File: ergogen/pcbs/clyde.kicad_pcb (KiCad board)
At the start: 2 copper layers, 111.4 x 85.7 mm, 24 parts

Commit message: prototypes ordered
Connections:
- TRRS1 pad 4: GP12 -> GP16
- U0 pad 10: matrix_middle_home -> matrix_inner_home
- U0 pad 11: matrix_middle_bottom -> matrix_inner_bottom
- U0 pad 12: matrix_index_top -> matrix_ring_bottom
- U0 pad 14: matrix_index_home -> matrix_ring_home
- U0 pad 15: matrix_index_bottom -> matrix_ring_top
- U0 pad 16: GP12 -> matrix_middle_top
- U0 pad 17: matrix_inner_bottom -> matrix_middle_home
- U0 pad 19: matrix_inner_home -> matrix_middle_bottom
- U0 pad 20: matrix_inner_top -> GP15
- U0 pad 21: thumbfan_far_home -> GP16
- U0 pad 22: thumbfan_home_home -> thumbfan_far_home
- U0 pad 24: thumbfan_near_home -> thumbfan_home_home
- U0 pad 25: GP19 -> thumbfan_near_home
- U0 pad 5: matrix_ring_bottom -> matrix_index_bottom
- U0 pad 6: matrix_ring_home -> matrix_index_home
- U0 pad 7: matrix_ring_top -> matrix_index_top
- U0 pad 9: matrix_middle_top -> matrix_inner_top
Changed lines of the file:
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@@
 (net 18 "thumbfan_home_home")
 (net 19 "thumbfan_far_home")
-(net 20 "GP12")
-(net 21 "GP19")
+(net 20 "GP15")
+(net 21 "GP16")
 (net 22 "GP20")
 (net 23 "GP21")
@@
 (add_net "thumbfan_home_home")
 (add_net "thumbfan_far_home")
-(add_net "GP12")
-(add_net "GP19")
+(add_net "GP15")
+(add_net "GP16")
 (add_net "GP20")
 (add_net "GP21")
@@
     (pad "3" thru_hole rect (at 8.82 -19.05) (size 1.84 1.7) (drill oval 1.16 1.02) (layers *.Cu *.Mask) (net 2 "GND"))
     (pad "4" thru_hole oval (at 8.82 -16.51) (size 1.84 1.7) (drill oval 1.16 1.02) (layers *.Cu *.Mask) (net 1 "matrix_pinky_bottom"))
-    (pad "5" thru_hole oval (at 8.82 -13.97) (size 1.84 1.7) (drill oval 1.16 1.02) (layers *.Cu *.Mask) (net 5 "matrix_ring_bottom"))
-    (pad "6" thru_hole oval (at 8.82 -11.43) (size 1.84 1.7) (drill oval 1.16 1.02) (layers *.Cu *.Mask) (net 6 "matrix_ring_home"))
-    (pad "7" thru_hole oval (at 8.82 -8.89) (size 1.84 1.7) (drill oval 1.16 1.02) (layers *.Cu *.Mask) (net 7 "matrix_ring_top"))
+    (pad "5" thru_hole oval (at 8.82 -13.97) (size 1.84 1.7) (drill oval 1.16 1.02) (layers *.Cu *.Mask) (net 11 "matrix_index_bottom"))
+    (pad "6" thru_hole oval (at 8.82 -11.43) (size 1.84 1.7) (drill oval 1.16 1.02) (layers *.Cu *.Mask) (net 12 "matrix_index_home"))
+    (pad "7" thru_hole oval (at 8.82 -8.89) (size 1.84 1.7) (drill oval 1.16 1.02) (layers *.Cu *.Mask) (net 13 "matrix_index_top"))
     (pad "8" thru_hole rect (at 8.82 -6.35) (size 1.84 1.7) (drill oval 1.16 1.02) (layers *.Cu *.Mask) (net 2 "GND"))
-    (pad "9" thru_hole oval (at 8.82 -3.81) (size 1.84 1.7) (drill oval 1.16 1.02) (layers *.Cu *.Mask) (net 10 "matrix_middle_top"))
-    (pad "10" thru_hole oval (at 8.82 -1.27) (size 1.84 1.7) (drill oval 1.16 1.02) (layers *.Cu *.Mask) (net 9 "matrix_middle_home"))
-    (pad "11" thru_hole oval (at 8.82 1.27) (size 1.84 1.7) (drill oval 1.16 1.02) (layers *.Cu *.Mask) (net 8 "matrix_middle_bottom"))
-    (pad "12" thru_hole oval (at 8.82 3.81) (size 1.84 1.7) (drill oval 1.16 1.02) (layers *.Cu *.Mask) (net 13 "matrix_index_top"))
+    (pad "9" thru_hole oval (at 8.82 -3.81) (size 1.84 1.7) (drill oval 1.16 1.02) (layers *.Cu *.Mask) (net 16 "matrix_inner_top"))
+    (pad "10" thru_hole oval (at 8.82 -1.27) (size 1.84 1.7) (drill oval 1.16 1.02) (layers *.Cu *.Mask) (net 15 "matrix_inner_home"))
+    (pad "11" thru_hole oval (at 8.82 1.27) (size 1.84 1.7) (drill oval 1.16 1.02) (layers *.Cu *.Mask) (net 14 "matrix_inner_bottom"))
+    (pad "12" thru_hole oval (at 8.82 3.81) (size 1.84 1.7) (drill oval 1.16 1.02) (layers *.Cu *.Mask) (net 5 "matrix_ring_bottom"))
     (pad "13" thru_hole rect (at 8.82 6.35) (size 1.84 1.7) (drill oval 1.16 1.02) (layers *.Cu *.Mask) (net 2 "GND"))
-    (pad "14" thru_hole oval (at 8.82 8.89) (size 1.84 1.7) (drill oval 1.16 1.02) (layers *.Cu *.Mask) (net 12 "matrix_index_home"))
-    (pad "15" thru_hole oval (at 8.82 11.43) (size 1.84 1.7) (drill oval 1.16 1.02) (layers *.Cu *.Mask) (net 11 "matrix_index_bottom"))
-    (pad "16" thru_hole oval (at 8.82 13.97) (size 1.84 1.7) (drill oval 1.16 1.02) (layers *.Cu *.Mask) (net 20 "GP12"))
-    (pad "17" thru_hole oval (at 8.82 16.51) (size 1.84 1.7) (drill oval 1.16 1.02) (layers *.Cu *.Mask) (net 14 "matrix_inner_bottom"))
+    (pad "14" thru_hole oval (at 8.82 8.89) (size 1.84 1.7) (drill oval 1.16 1.02) (layers *.Cu *.Mask) (net 6 "matrix_ring_home"))
+    (pad "15" thru_hole oval (at 8.82 11.43) (size 1.84 1.7) (drill oval 1.16 1.02) (layers *.Cu *.Mask) (net 7 "matrix_ring_top"))
+    (pad "16" thru_hole oval (at 8.82 13.97) (size 1.84 1.7) (drill oval 1.16 1.02) (layers *.Cu *.Mask) (net 10 "matrix_middle_top"))
+    (pad "17" thru_hole oval (at 8.82 16.51) (size 1.84 1.7) (drill oval 1.16 1.02) (layers *.Cu *.Mask) (net 9 "matrix_middle_home"))
     (pad "18" thru_hole rect (at 8.82 19.05) (size 1.84 1.7) (drill oval 1.16 1.02) (layers *.Cu *.Mask) (net 2 "GND"))
-    (pad "19" thru_hole oval (at 8.82 21.59) (size 1.84 1.7) (drill oval 1.16 1.02) (layers *.Cu *.Mask) (net 15 "matrix_inner_home"))
-    (pad "20" thru_hole oval (at 8.82 24.13) (size 1.84 1.7) (drill oval 1.16 1.02) (layers *.Cu *.Mask) (net 16 "matrix_inner_top"))
-    (pad "21" thru_hole oval (at -8.82 24.13) (size 1.84 1.7) (drill oval 1.16 1.02) (layers *.Cu *.Mask) (net 19 "thumbfan_far_home"))
-    (pad "22" thru_hole oval (at -8.82 21.59) (size 1.84 1.7) (drill oval 1.16 1.02) (layers *.Cu *.Mask) (net 18 "thumbfan_home_home"))
+    (pad "19" thru_hole oval (at 8.82 21.59) (size 1.84 1.7) (drill oval 1.16 1.02) (layers *.Cu *.Mask) (net 8 "matrix_middle_bottom"))
+    (pad "20" thru_hole oval (at 8.82 24.13) (size 1.84 1.7) (drill oval 1.16 1.02) (layers *.Cu *.Mask) (net 20 "GP15"))
+    (pad "21" thru_hole oval (at -8.82 24.13) (size 1.84 1.7) (drill oval 1.16 1.02) (layers *.Cu *.Mask) (net 21 "GP16"))
+    (pad "22" thru_hole oval (at -8.82 21.59) (size 1.84 1.7) (drill oval 1.16 1.02) (layers *.Cu *.Mask) (net 19 "thumbfan_far_home"))
     (pad "23" thru_hole rect (at -8.82 19.05) (size 1.84 1.7) (drill oval 1.16 1.02) (layers *.Cu *.Mask) (net 2 "GND"))
-    (pad "24" thru_hole oval (at -8.82 16.51) (size 1.84 1.7) (drill oval 1.16 1.02) (layers *.Cu *.Mask) (net 17 "thumbfan_near_home"))
-    (pad "25" thru_hole oval (at -8.82 13.97) (size 1.84 1.7) (drill oval 1.16 1.02) (layers *.Cu *.Mask) (net 21 "GP19"))
+    (pad "24" thru_hole oval (at -8.82 16.51) (size 1.84 1.7) (drill oval 1.16 1.02) (layers *.Cu *.Mask) (net 18 "thumbfan_home_home"))
+    (pad "25" thru_hole oval (at -8.82 13.97) (size 1.84 1.7) (drill oval 1.16 1.02) (layers *.Cu *.Mask) (net 17 "thumbfan_near_home"))
     (pad "26" thru_hole oval (at -8.82 11.43) (size 1.84 1.7) (drill oval 1.16 1.02) (layers *.Cu *.Mask) (net 22 "GP20"))
     (pad "27" thru_hole oval (at -8.82 8.89) (size 1.84 1.7) (drill oval 1.16 1.02) (layers *.Cu *.Mask) (net 23 "GP21"))
@@
         (pad 2 thru_hole oval (at -4.6 10.2 0) (size 1.6 2.2) (drill oval 0.9 1.5) (layers *.Cu *.Mask) (net 2 "GND"))
         (pad 3 thru_hole oval (at -4.6 6.2 0) (size 1.6 2.2) (drill oval 0.9 1.5) (layers *.Cu *.Mask) (net 32 "VSYS"))
-        (pad 4 thru_hole oval (at -4.6 3.2 0) (size 1.6 2.2) (drill oval 0.9 1.5) (layers *.Cu *.Mask) (net 20 "GP12"))
+        (pad 4 thru_hole oval (at -4.6 3.2 0) (size 1.6 2.2) (drill oval 0.9 1.5) (layers *.Cu *.Mask) (net 21 "GP16"))
         (pad 1 thru_hole oval (at -4.6 11.3 0) (size 1.6 2.2) (drill oval 0.9 1.5) (layers *.Cu *.Mask) (net 2 "GND"))
         (pad 2 thru_hole oval (at 0 10.2 0) (size 1.6 2.2) (drill oval 0.9 1.5) (layers *.Cu *.Mask) (net 2 "GND"))
         (pad 3 thru_hole oval (at 0 6.2 0) (size 1.6 2.2) (drill oval 0.9 1.5) (layers *.Cu *.Mask) (net 32 "VSYS"))
-        (pad 4 thru_hole oval (at 0 3.2 0) (size 1.6 2.2) (drill oval 0.9 1.5) (layers *.Cu *.Mask) (net 20 "GP12"))
+        (pad 4 thru_hole oval (at 0 3.2 0) (size 1.6 2.2) (drill oval 0.9 1.5) (layers *.Cu *.Mask) (net 21 "GP16"))
       )
             (gr_text "JLCJLCJLCJLC" (at 190.5 123.825 0) (layer F.SilkS)

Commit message: layout like split weteor/Kong; outline tweaks
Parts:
- moved S16 4.76 mm to (209.6, 175.3)
- moved S17 4.76 mm to (228.6, 175.3)
- moved _4 4.76 mm to (238.1, 165.7)
- moved S18 4.39 mm to (247.7, 177.6)
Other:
- board size 111.4 x 85.7 mm -> 114.3 x 82.4 mm
- board text added: "clyde v0.0.2"
- board text removed: "clyde v0.0.1"
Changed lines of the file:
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@@
           )
       (module MX (layer F.Cu)
-      (at 206.69250000000002 179.07 0)
+      (at 209.55 175.26 0)
       (fp_text reference "S16" (at 0 0) (layer F.SilkS) hide (effects (font (size 1.27 1.27) (thickness 0.15))))
       (fp_text value "" (at 0 0) (layer F.SilkS) hide (effects (font (size 1.27 1.27) (thickness 0.15))))
@@
           )
       (module MX (layer F.Cu)
-      (at 225.74250000000004 179.07 0)
+      (at 228.60000000000002 175.26 0)
       (fp_text reference "S17" (at 0 0) (layer F.SilkS) hide (effects (font (size 1.27 1.27) (thickness 0.15))))
       (fp_text value "" (at 0 0) (layer F.SilkS) hide (effects (font (size 1.27 1.27) (thickness 0.15))))
@@
           )
       (module MX (layer F.Cu)
-      (at 244.79250000000002 180.975 0)
+      (at 247.65 177.64124999999999 0)
       (fp_text reference "S18" (at 0 0) (layer F.SilkS) hide (effects (font (size 1.27 1.27) (thickness 0.15))))
       (fp_text value "" (at 0 0) (layer F.SilkS) hide (effects (font (size 1.27 1.27) (thickness 0.15))))
@@
                 (effects (font (size 1 1) (thickness 0.15)) )
             )
-            (gr_text "clyde v0.0.1" (at 190.5 142.875 0) (layer F.SilkS)
+            (gr_text "clyde v0.0.2" (at 190.5 142.875 0) (layer F.SilkS)
                 (effects (font (size 1 1) (thickness 0.15)) )
             )
     (module "MountingHole_2.2mm_M2_Pad_Via" (version 20210722) (generator pcbnew) (layer "F.Cu")
-      (at 235.26750000000004 169.545 0)
+      (at 238.12500000000003 165.73499999999999 0)
       (fp_text reference "_4" (at 0 -3.2) (layer "F.SilkS") hide
         (effects (font (size 1 1) (thickness 0.15)))
@@
       (pad "1" thru_hole circle locked (at 0 -1.65) (size 0.7 0.7) (drill 0.4) (layers *.Cu *.Mask))
     )
-            (gr_line (start 142.875 182.88815625463917) (end 142.875 107.77499999999999) (angle 90) (layer Edge.Cuts) (width 0.15))
-(gr_line (start 145.875 104.77499999999999) (end 244.94297008970588 104.77499999999999) (angle 90) (layer Edge.Cuts) (width 0.15))
-(gr_line (start 247.92719999989208 107.46779999895125) (end 254.30172991018622 169.3918048418086) (angle 90) (layer Edge.Cuts) (width 0.15))
-(gr_line (start 254.31750000000002 169.699004842857) (end 254.31750000000002 187.5) (angle 90) (layer Edge.Cuts) (width 0.15))
-(gr_line (start 251.31750000000002 190.5) (end 235.34476865999997 190.5) (angle 90) (layer Edge.Cuts) (width 0.15))
-(gr_line (start 235.19033465459398 190.49602240487596) (end 145.720565994594 185.8841786595152) (angle 90) (layer Edge.Cuts) (width 0.15))
-(gr_arc (start 145.875 107.77499999999999) (end 145.875 104.77499999999999) (angle -90) (layer Edge.Cuts) (width 0.15))
-(gr_arc (start 244.94297008970588 107.77499999999999) (end 247.92719998970588 107.4678) (angle -84.1226099916367) (layer Edge.Cuts) (width 0.15))
-(gr_arc (start 251.31750000000002 169.699004842857) (end 254.31750000000002 169.699004842857) (angle -5.877390008356565) (layer Edge.Cuts) (width 0.15))
-(gr_arc (start 251.31750000000002 187.5) (end 251.31750000000002 190.5) (angle -90) (layer Edge.Cuts) (width 0.15))
-(gr_arc (start 235.34476865999997 187.5) (end 235.19033465999996 190.4960224) (angle -2.9507764544792394) (layer Edge.Cuts) (width 0.15))
-(gr_arc (start 145.875 182.88815625463917) (end 142.875 182.88815625463917) (angle -87.04922354552087) (layer Edge.Cuts) (width 0.15))
+            (gr_line (start 142.875 185.16625) (end 142.875 106.77499999999999) (angle 90) (layer Edge.Cuts) (width 0.15))
+(gr_line (start 144.875 104.77499999999999) (end 245.65000000000003 104.77499999999999) (angle 90) (layer Edge.Cuts) (width 0.15))
+(gr_line (start 247.65000000000003 106.77499999999999) (end 247.65000000000003 166.11624999999998) (angle 90) (layer Edge.Cuts) (width 0.15))
+(gr_line (start 249.65000000000003 168.11624999999998) (end 255.175 168.11624999999998) (angle 90) (layer Edge.Cuts) (width 0.15))
+(gr_line (start 257.175 170.11624999999998) (end 257.175 185.16625) (angle 90) (layer Edge.Cuts) (width 0.15))
+(gr_line (start 255.175 187.16625) (end 144.875 187.16625) (angle 90) (layer Edge.Cuts) (width 0.15))
+(gr_arc (start 144.875 106.77499999999999) (end 144.875 104.77499999999999) (angle -90) (layer Edge.Cuts) (width 0.15))
+(gr_arc (start 245.65000000000003 106.77499999999999) (end 247.65000000000003 106.77499999999999) (angle -90) (layer Edge.Cuts) (width 0.15))
+(gr_arc (start 249.65000000000003 166.11624999999998) (end 247.65000000000003 166.11624999999998) (angle -90) (layer Edge.Cuts) (width 0.15))
+(gr_arc (start 255.175 170.11624999999998) (end 257.175 170.11624999999998) (angle -90) (layer Edge.Cuts) (width 0.15))
+(gr_arc (start 255.175 185.16625) (end 255.175 187.16625) (angle -90) (layer Edge.Cuts) (width 0.15))
+(gr_arc (start 144.875 185.16625) (end 142.875 185.16625) (angle -90) (layer Edge.Cuts) (width 0.15))
 )

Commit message: begin work on v1
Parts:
- added _8: , MountingHole_2.2mm_M2_Pad_Via, F.Cu at (219.1, 142.9)
- U0: footprint RPi_Pico_TH_oval_face_down -> RPi_Pico_TH_oval_face_up
- moved U0 90.4 mm to (248.6, 131.3), turned to 0 degrees
- moved TRRS1 60.3 mm to (257.2, 163.8), turned to 270 degrees
- moved _5 50.4 mm to (161.9, 123.8)
- moved _6 19.1 mm to (161.9, 142.9)
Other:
- board size 114.3 x 82.4 mm -> 116.2 x 82.4 mm
- board text added: "clyde v1.0.0"
- board text removed: "clyde v0.0.2"

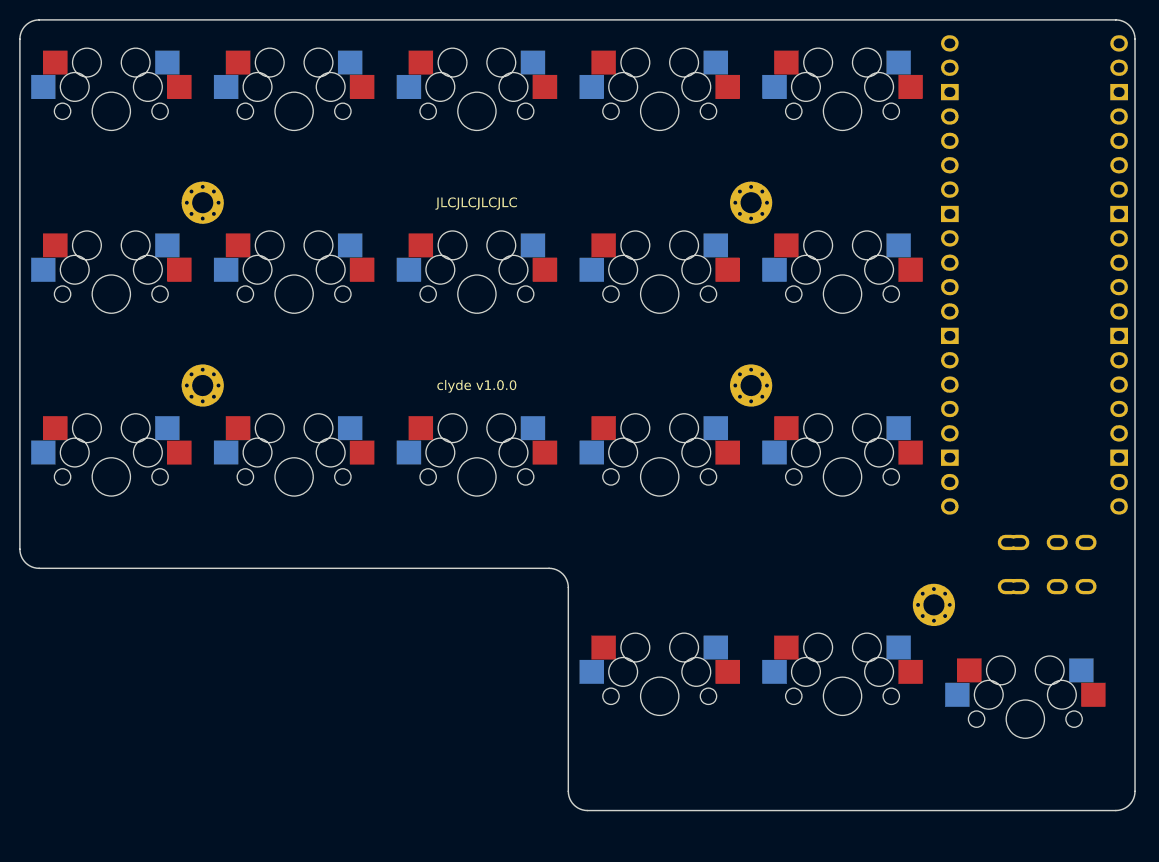
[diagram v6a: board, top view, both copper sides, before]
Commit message: working on plate case
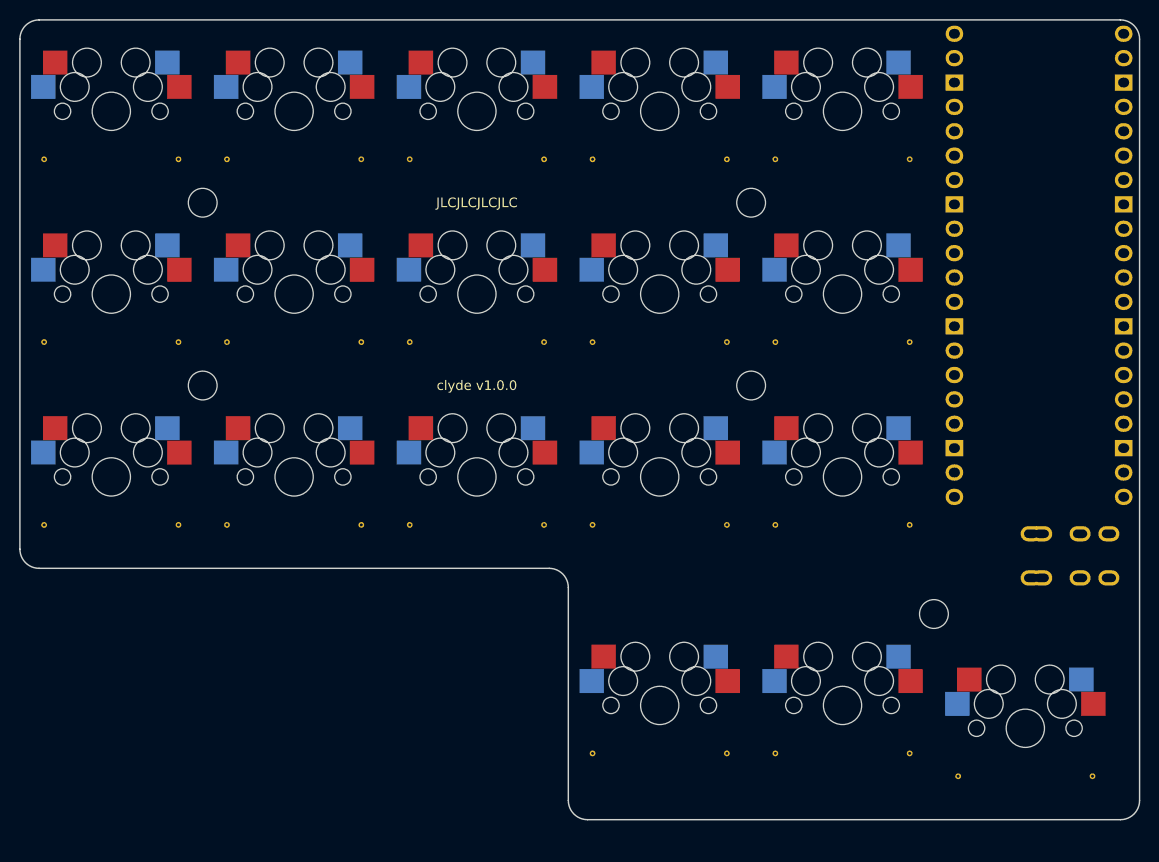
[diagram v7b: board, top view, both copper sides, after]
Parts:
- removed _4, _5, _6, _7, _8: , MountingHole_2.2mm_M2_Pad_Via
- added ?: , DrillHole, F.Cu at (238.1, 166.7)
- added ?: , DrillHole, F.Cu at (161.9, 123.8)
- added ?: , DrillHole, F.Cu at (161.9, 142.9)
- added ?: , DrillHole, F.Cu at (219.1, 123.8)
- added ?: , DrillHole, F.Cu at (219.1, 142.9)
- added REF**: VIA-0.6mm, VIA-0.6mm, F.Cu at (145.4, 157.4)
- added REF**: VIA-0.6mm, VIA-0.6mm, F.Cu at (202.6, 157.4)
- added REF**: VIA-0.6mm, VIA-0.6mm, F.Cu at (202.6, 138.3)
- added REF**: VIA-0.6mm, VIA-0.6mm, F.Cu at (202.6, 119.3)
- added REF**: VIA-0.6mm, VIA-0.6mm, F.Cu at (221.6, 157.4)
- added REF**: VIA-0.6mm, VIA-0.6mm, F.Cu at (221.6, 138.3)
- added REF**: VIA-0.6mm, VIA-0.6mm, F.Cu at (221.6, 119.3)
- added REF**: VIA-0.6mm, VIA-0.6mm, F.Cu at (202.6, 181.2)
- added REF**: VIA-0.6mm, VIA-0.6mm, F.Cu at (221.6, 181.2)
- added REF**: VIA-0.6mm, VIA-0.6mm, F.Cu at (240.7, 183.6)
- added REF**: VIA-0.6mm, VIA-0.6mm, F.Cu at (159.4, 157.4)
- added REF**: VIA-0.6mm, VIA-0.6mm, F.Cu at (145.4, 138.3)
- added REF**: VIA-0.6mm, VIA-0.6mm, F.Cu at (159.4, 138.3)
- added REF**: VIA-0.6mm, VIA-0.6mm, F.Cu at (159.4, 119.3)
- added REF**: VIA-0.6mm, VIA-0.6mm, F.Cu at (178.5, 157.4)
- added REF**: VIA-0.6mm, VIA-0.6mm, F.Cu at (178.5, 138.3)
- added REF**: VIA-0.6mm, VIA-0.6mm, F.Cu at (178.5, 119.3)
- added REF**: VIA-0.6mm, VIA-0.6mm, F.Cu at (197.5, 157.4)
- added REF**: VIA-0.6mm, VIA-0.6mm, F.Cu at (197.5, 138.3)
- added REF**: VIA-0.6mm, VIA-0.6mm, F.Cu at (197.5, 119.3)
- added REF**: VIA-0.6mm, VIA-0.6mm, F.Cu at (216.6, 157.4)
- added REF**: VIA-0.6mm, VIA-0.6mm, F.Cu at (216.6, 138.3)
- added REF**: VIA-0.6mm, VIA-0.6mm, F.Cu at (145.4, 119.3)
- added REF**: VIA-0.6mm, VIA-0.6mm, F.Cu at (216.6, 119.3)
- added REF**: VIA-0.6mm, VIA-0.6mm, F.Cu at (235.6, 157.4)
- added REF**: VIA-0.6mm, VIA-0.6mm, F.Cu at (235.6, 138.3)
- added REF**: VIA-0.6mm, VIA-0.6mm, F.Cu at (235.6, 119.3)
- added REF**: VIA-0.6mm, VIA-0.6mm, F.Cu at (216.6, 181.2)
- added REF**: VIA-0.6mm, VIA-0.6mm, F.Cu at (235.6, 181.2)
- added REF**: VIA-0.6mm, VIA-0.6mm, F.Cu at (254.7, 183.6)
- added REF**: VIA-0.6mm, VIA-0.6mm, F.Cu at (164.5, 157.4)
- added REF**: VIA-0.6mm, VIA-0.6mm, F.Cu at (164.5, 138.3)
- added REF**: VIA-0.6mm, VIA-0.6mm, F.Cu at (164.5, 119.3)
- added REF**: VIA-0.6mm, VIA-0.6mm, F.Cu at (183.5, 157.4)
- added REF**: VIA-0.6mm, VIA-0.6mm, F.Cu at (183.5, 138.3)
- added REF**: VIA-0.6mm, VIA-0.6mm, F.Cu at (183.5, 119.3)
- moved TRRS1 2.55 mm to (259.6, 162.9)
- moved U0 1.11 mm to (249.1, 130.3)
- moved S16 0.95 mm to (209.6, 176.2)
- moved S17 0.95 mm to (228.6, 176.2)
- moved S18 0.95 mm to (247.7, 178.6)
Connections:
- net thumbfan_far_home renamed thumb_far_mods
- net thumbfan_home_home renamed thumb_middle_mods
- net thumbfan_near_home renamed thumb_near_mods
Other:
- board size 116.2 x 82.4 mm -> 116.7 x 83.3 mm
